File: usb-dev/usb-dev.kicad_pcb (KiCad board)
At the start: 4 copper layers, 32 x 32 mm, 42 parts, among them J1 HS USB, J2 FS USB, J3 Conn_02x05_Odd_Even, J4 Conn_02x05_Odd_Even, J5 Molex_104031-0811, J6 Conn_01x06_Male, SW1 SW_Push, SW2 SW_Push, SW3 SW_Push, U1 LPC55x16JEV98E, U2 AP2127K-3.3, Y1 ABM8-16.000MHZ-B2-T

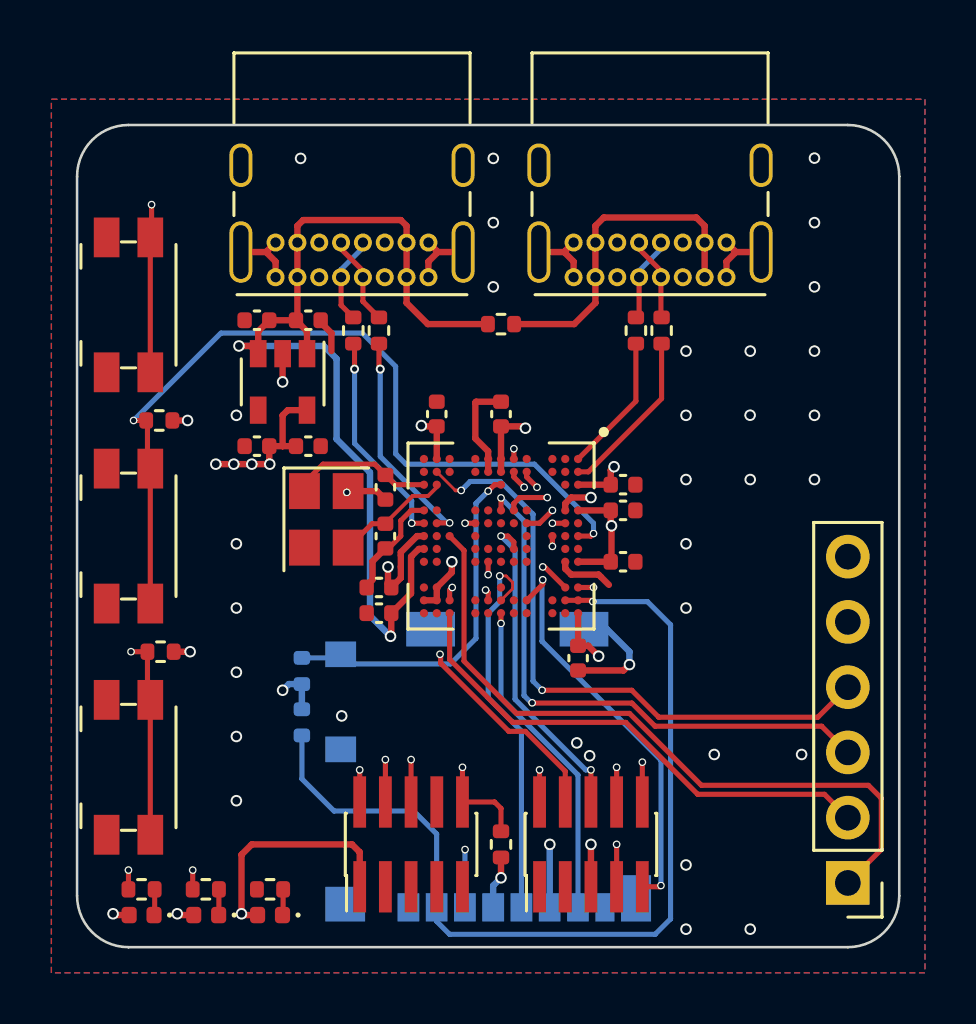
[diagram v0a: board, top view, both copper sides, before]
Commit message: Fixed VDD_PMU, added fet to SD power and added extra CS line to SPI header
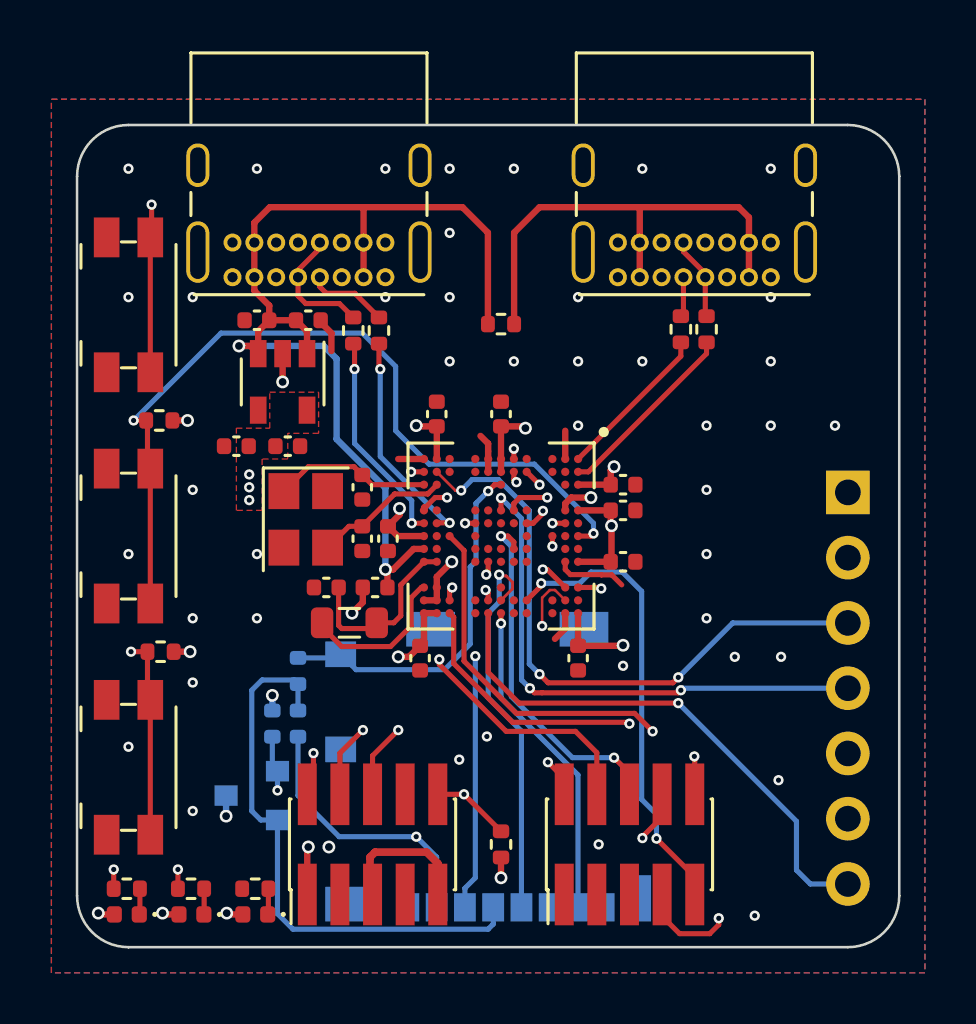
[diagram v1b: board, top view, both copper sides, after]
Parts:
- added C14: 22u, Capacitor_SMD:C_0402_1005Metric, F.Cu at (124.7, 78.0)
- added C16: 0.1u, Capacitor_SMD:C_0402_1005Metric, F.Cu at (128.3, 80.8)
- added L1: 4.7u, Inductor_SMD:L_0805_2012Metric, F.Cu at (125.6, 79.4)
- added Q1: DMP3099L, Package_TO_SOT_SMD:SOT-23, B.Cu at (121.8, 86.1)
- added R11: 10k, Resistor_SMD:R_0402_1005Metric, B.Cu at (122.6, 83.3)
- J3, J4: footprint Connector_PinHeader_1.00mm:PinHeader_2x05_P1.00mm_Vertical_SMD -> Connector_PinHeader_1.27mm:PinHeader_2x05_P1.27mm_Vertical_SMD
- J6: value Conn_01x06_Male -> Conn_01x07_Male; footprint Connector_PinHeader_2.54mm:PinHeader_1x06_P2.54mm_Vertical -> Connector_PinHeader_2.54mm:PinHeader_1x07_P2.54mm_Vertical; moved to B.Cu
- moved J6 15.2 mm to (145.0, 74.3)
- moved C2 1.93 mm to (127.1, 76.1), turned to 90 degrees
- moved R5 1.75 mm to (138.5, 68.0)
- moved R6 1.75 mm to (139.5, 68.0)
- moved J2 1.72 mm to (142.0, 65.9)
- moved J1 1.68 mm to (127.0, 65.9)
- moved J3 1.50 mm to (126.5, 88.0)
- moved J4 1.50 mm to (136.5, 88.0)
- moved C7 1.01 mm to (126.6, 78.0)
- moved C15 0.91 mm to (126.1, 76.1)
- moved C13 0.90 mm to (126.1, 74.1)
- moved C11 0.80 mm to (121.2, 72.5)
- moved C12 0.80 mm to (123.2, 72.5)
- moved Y1 0.80 mm to (123.9, 75.3)
- moved D2 0.58 mm to (121.9, 90.7)
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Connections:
- J5 pad 4: +3V3 -> Net-(J5-Pad4)
- J6 pad 1: /SPI_CS -> GND
- J6 pad 2: /SPI_CIPO -> +3V3
- J6 pad 3: /SPI_CLK -> /SPI_COPI
- J6 pad 4: /SPI_COPI -> /SPI_CLK
- J6 pad 5: +3V3 -> /SPI_CIPO
- J6 pad 6: GND -> /SPI_CS0
- R13 pad 2: +3V3 -> Net-(J5-Pad4)
- R7 pad 2: +3V3 -> Net-(J5-Pad4)
- U1 pad A12: /SD_CS -> unconnected-(U1-PadA12)
- U1 pad H13: unconnected-(U1-PadH13) -> /SPI_CS1
- U1 pad L7: /SPI_CS -> /SPI_CS0
- U1 pad M13: unconnected-(U1-PadM13) -> +3V3
- U1 pad M9: unconnected-(U1-PadM9) -> Net-(C14-Pad2)
- U1 pad N11: unconnected-(U1-PadN11) -> Net-(L1-Pad2)
- U1 pad N13: unconnected-(U1-PadN13) -> +3V3
- U1 pad N2: unconnected-(U1-PadN2) -> /SD_PWR_nEN
- U1 pad N9: unconnected-(U1-PadN9) -> Net-(C14-Pad2)
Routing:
- net /SPI_CS: track 27.4 -> 0.00 mm
- net /SPI_CS0: track 0.00 -> 22.6 mm, vias 0 -> 1
- net Net-(J5-Pad4): track 0.00 -> 21.9 mm
- net /SPI_CS1: track 0.00 -> 20.8 mm, vias 0 -> 1
- net /SD_PWR_nEN: track 0.00 -> 17.2 mm, vias 0 -> 2
- net GND: track 37.5 -> 22.1 mm, vias 39 -> 48
- net /SD_CS: track 36.7 -> 24.2 mm, vias 1 -> 2
- net +3V3: track 38.7 -> 26.9 mm, vias 17 -> 19
- net Net-(C14-Pad2): track 0.00 -> 7.13 mm
- net Net-(L1-Pad2): track 0.00 -> 6.04 mm
- net /SD_COPI: track 18.5 -> 13.1 mm
- net /FS_VBUS: track 13.0 -> 18.3 mm
- net /TGT_UART_RX: track 15.6 -> 19.7 mm
- net /TGT_TDI: track 14.8 -> 18.5 mm
- net /TGT_UART_TX: track 15.7 -> 18.0 mm
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- added copper zone on F.Cu, net +3V3
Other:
- board text added: "CS0"
- board text added: "CS1"
- board text added: "usb-dev r0.2"
- board text removed: "CS"
- board text removed: "usb-dev r0.1"

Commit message: Fixed missing VDDCORE connections to internal switcher D:
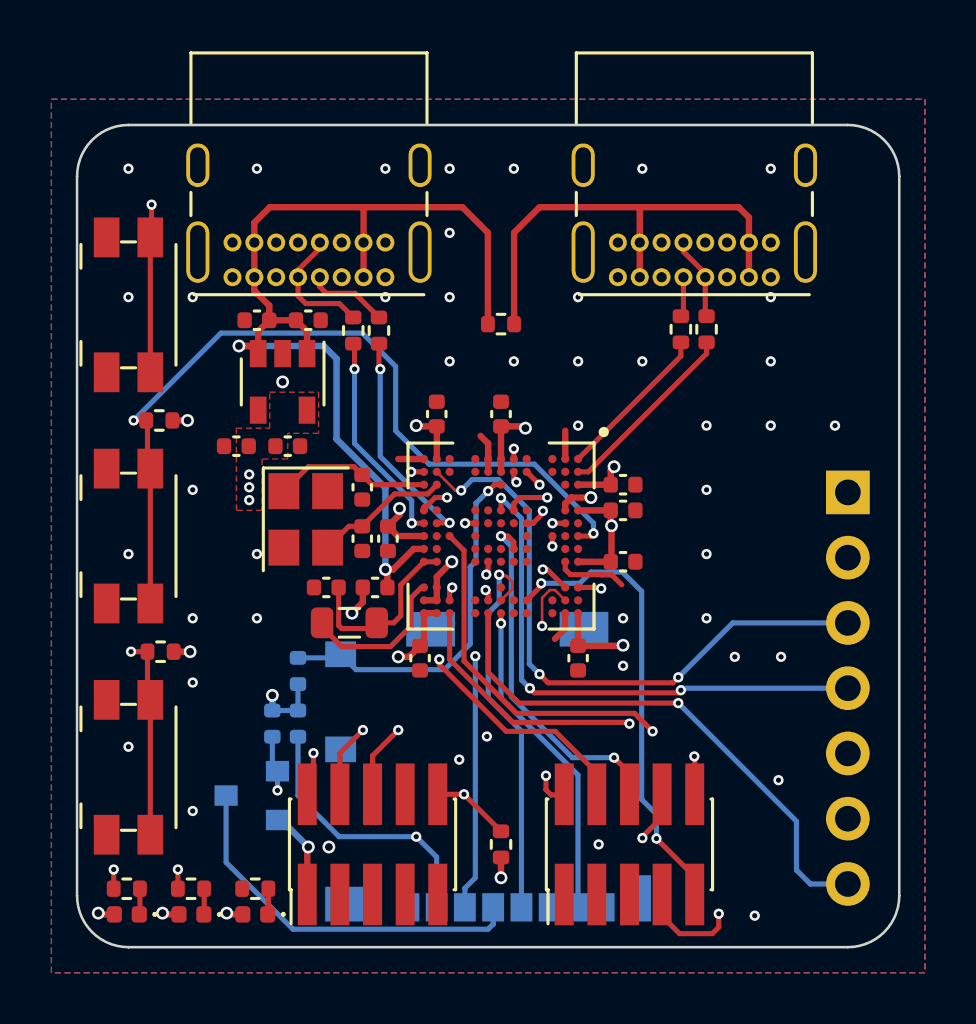
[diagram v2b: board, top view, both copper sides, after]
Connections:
- Q1 pad 2: Net-(J5-Pad4) -> +3V3
- Q1 pad 3: +3V3 -> Net-(J5-Pad4)
- R13 pad 2: Net-(J5-Pad4) -> +3V3
- R7 pad 2: Net-(J5-Pad4) -> +3V3
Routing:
- net GND: track 22.1 -> 14.1 mm, vias 48 -> 49
- net Net-(J5-Pad4): track 21.9 -> 14.8 mm
- net +3V3: track 26.9 -> 29.8 mm, vias 19 -> 18
